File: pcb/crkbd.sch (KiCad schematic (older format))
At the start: 79 parts, among them J1 MJ-4PP-9, J2 OLED, J3 LED, SW1 SW_PUSH, SW10 SW_PUSH, SW11 SW_PUSH, SW12 SW_PUSH, SW13 SW_PUSH, SW14 SW_PUSH, SW15 SW_PUSH, SW16 SW_PUSH, SW17 SW_PUSH, SW18 SW_PUSH, SW19 SW_PUSH, SW2 SW_PUSH, SW20 SW_PUSH, SW21 SW_PUSH, SW3 SW_PUSH, SW4 SW_PUSH, SW5 SW_PUSH, SW6 SW_PUSH, SW7 SW_PUSH, SW8 SW_PUSH, SW9 SW_PUSH, U1 ProMicro

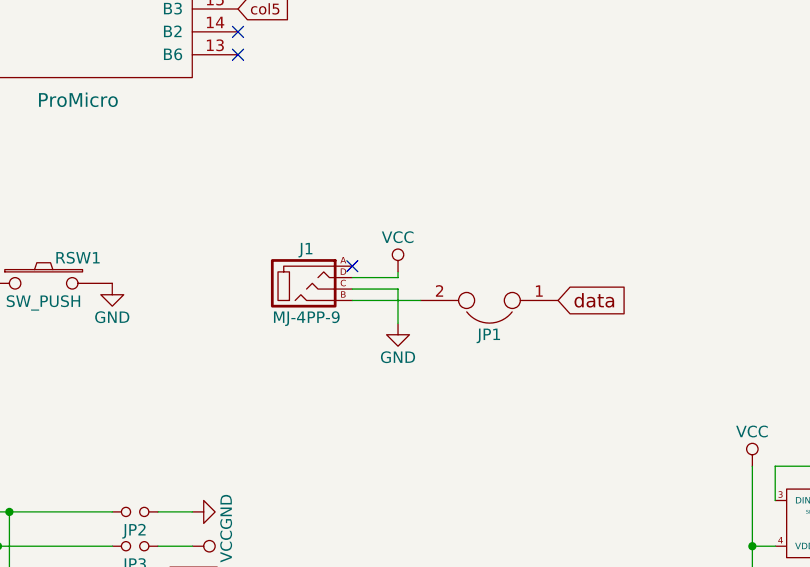
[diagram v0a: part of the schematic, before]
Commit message: Add i2c pin
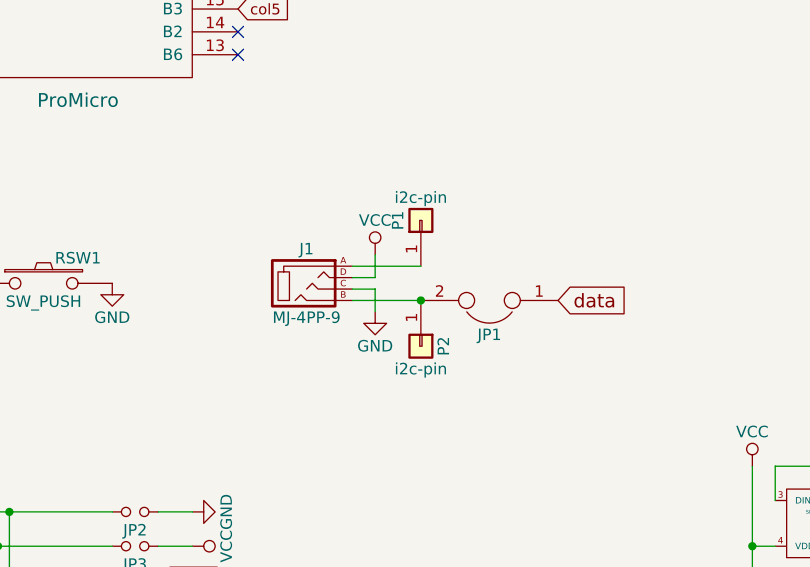
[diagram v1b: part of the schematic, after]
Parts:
- added P1, P2: i2c-pin, kbd:1pin_conn, symbol Conn_01x01
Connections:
- net at J1.B, JP1.2: now also P2.1 (Pin_1)
- net at J1.A: now also P1.1 (Pin_1)
- no-connect marks 7 -> 6
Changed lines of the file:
@@
 L VCC #PWR08
 U 1 1 5A76093E
-P 3200 3250
-F 0 "#PWR08" H 3200 3100 50  0001 C CNN
-F 1 "VCC" H 3200 3400 50  0000 C CNN
-F 2 "" H 3200 3250 50  0001 C CNN
-F 3 "" H 3200 3250 50  0001 C CNN
-	1    3200 3250
+P 3100 3175
+F 0 "#PWR08" H 3100 3025 50  0001 C CNN
+F 1 "VCC" H 3100 3325 50  0000 C CNN
+F 2 "" H 3100 3175 50  0001 C CNN
+F 3 "" H 3100 3175 50  0001 C CNN
+	1    3100 3175
 	1    0    0    -1
 $EndComp
@@
 L GND #PWR09
 U 1 1 5A760ADB
-P 3200 3475
-F 0 "#PWR09" H 3200 3225 50  0001 C CNN
-F 1 "GND" H 3200 3325 50  0000 C CNN
-F 2 "" H 3200 3475 50  0001 C CNN
-F 3 "" H 3200 3475 50  0001 C CNN
-	1    3200 3475
+P 3100 3425
+F 0 "#PWR09" H 3100 3175 50  0001 C CNN
+F 1 "GND" H 3100 3275 50  0000 C CNN
+F 2 "" H 3100 3425 50  0001 C CNN
+F 3 "" H 3100 3425 50  0001 C CNN
+	1    3100 3425
 	1    0    0    -1
 $EndComp
@@
 	1    0    0    -1
 $EndComp
-NoConn ~ 3000 3225
 Wire Wire Line
 	3000 3375 3300 3375
 Wire Wire Line
-	3000 3275 3200 3275
-Wire Wire Line
-	3200 3275 3200 3250
-Wire Wire Line
-	3000 3325 3200 3325
-Wire Wire Line
-	3200 3325 3200 3475
+	3000 3275 3100 3275
+Wire Wire Line
+	3100 3275 3100 3175
+Wire Wire Line
+	3000 3325 3100 3325
+Wire Wire Line
+	3100 3325 3100 3425
 $Comp
 L Conn_01x03 J3
@@
 Wire Wire Line
 	1375 6725 1525 6725
+$Comp
+L Conn_01x01 P2
+U 1 1 5AD20E0A
+P 3300 3575
+F 0 "P2" H 3300 3675 50  0000 C CNN
+F 1 "i2c-pin" V 3400 3575 50  0000 C CNN
+F 2 "kbd:1pin_conn" H 3300 3575 50  0001 C CNN
+F 3 "" H 3300 3575 50  0001 C CNN
+	1    3300 3575
+	0    1    1    0
+$EndComp
+$Comp
+L Conn_01x01 P1
+U 1 1 5AD21C5C
+P 3300 3025
+F 0 "P1" H 3300 3125 50  0000 C CNN
+F 1 "i2c-pin" V 3400 3025 50  0000 C CNN
+F 2 "kbd:1pin_conn" H 3300 3025 50  0001 C CNN
+F 3 "" H 3300 3025 50  0001 C CNN
+	1    3300 3025
+	0    -1   -1   0
+$EndComp
+Wire Wire Line
+	3000 3225 3300 3225
+Connection ~ 3300 3375
 $EndSCHEMATC

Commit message: Reset lines
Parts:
- RSW1: footprint kbd:SW_3.5x6.0_TH -> kbd:ResetSW
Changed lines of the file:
@@
 F 0 "RSW1" H 1800 3410 50  0000 C CNN
 F 1 "SW_PUSH" H 1650 3220 50  0000 C CNN
-F 2 "kbd:SW_3.5x6.0_TH" H 1650 3300 50  0001 C CNN
+F 2 "kbd:ResetSW" H 1650 3300 50  0001 C CNN
 F 3 "" H 1650 3300 50  0000 C CNN
 	1    1650 3300

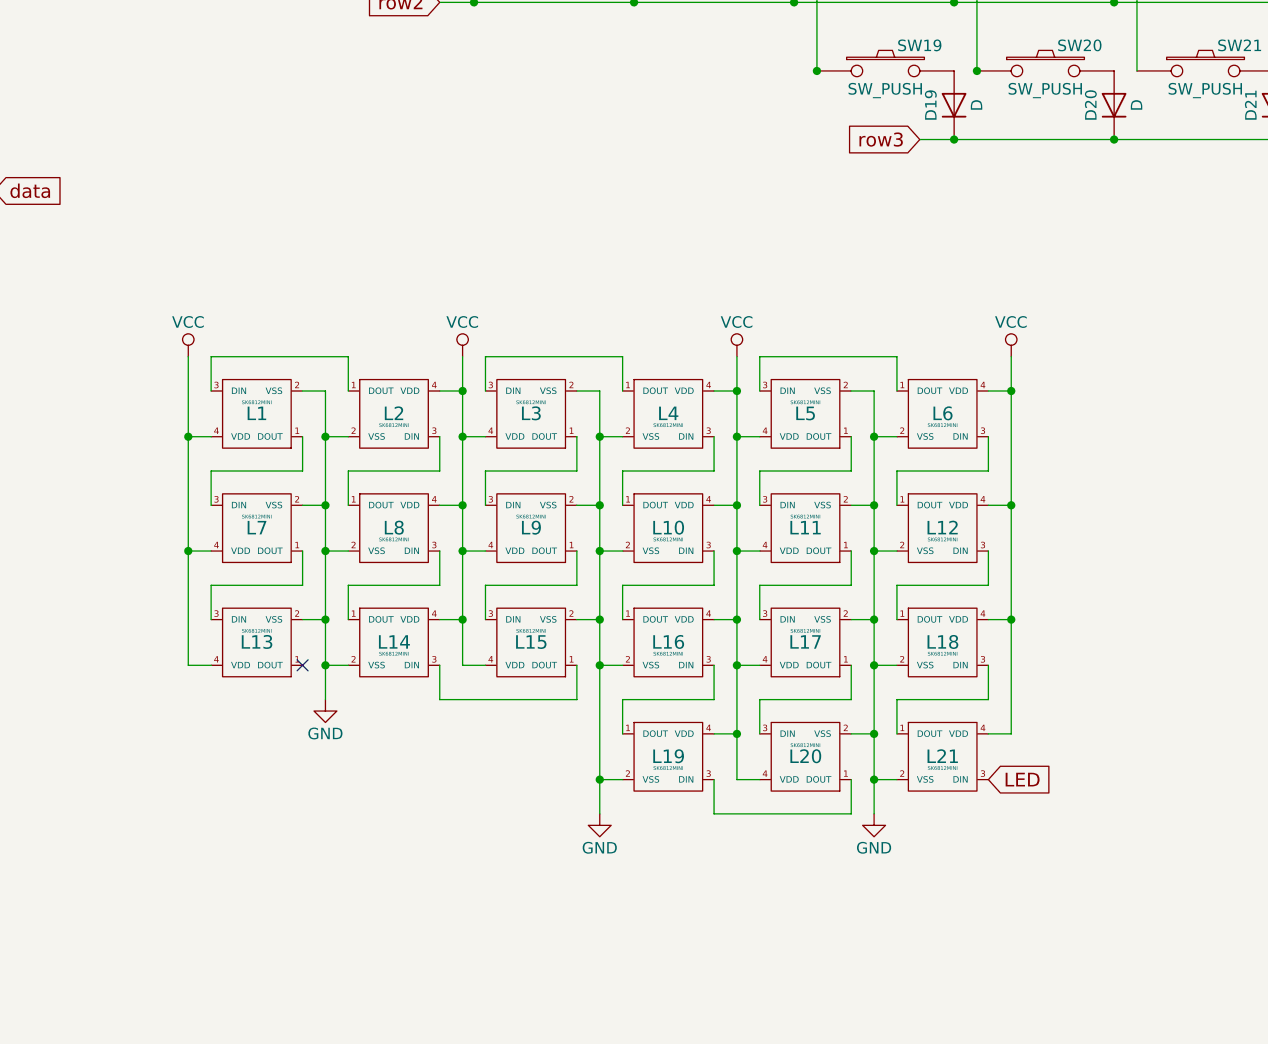
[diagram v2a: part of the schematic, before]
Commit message: Add underground leds
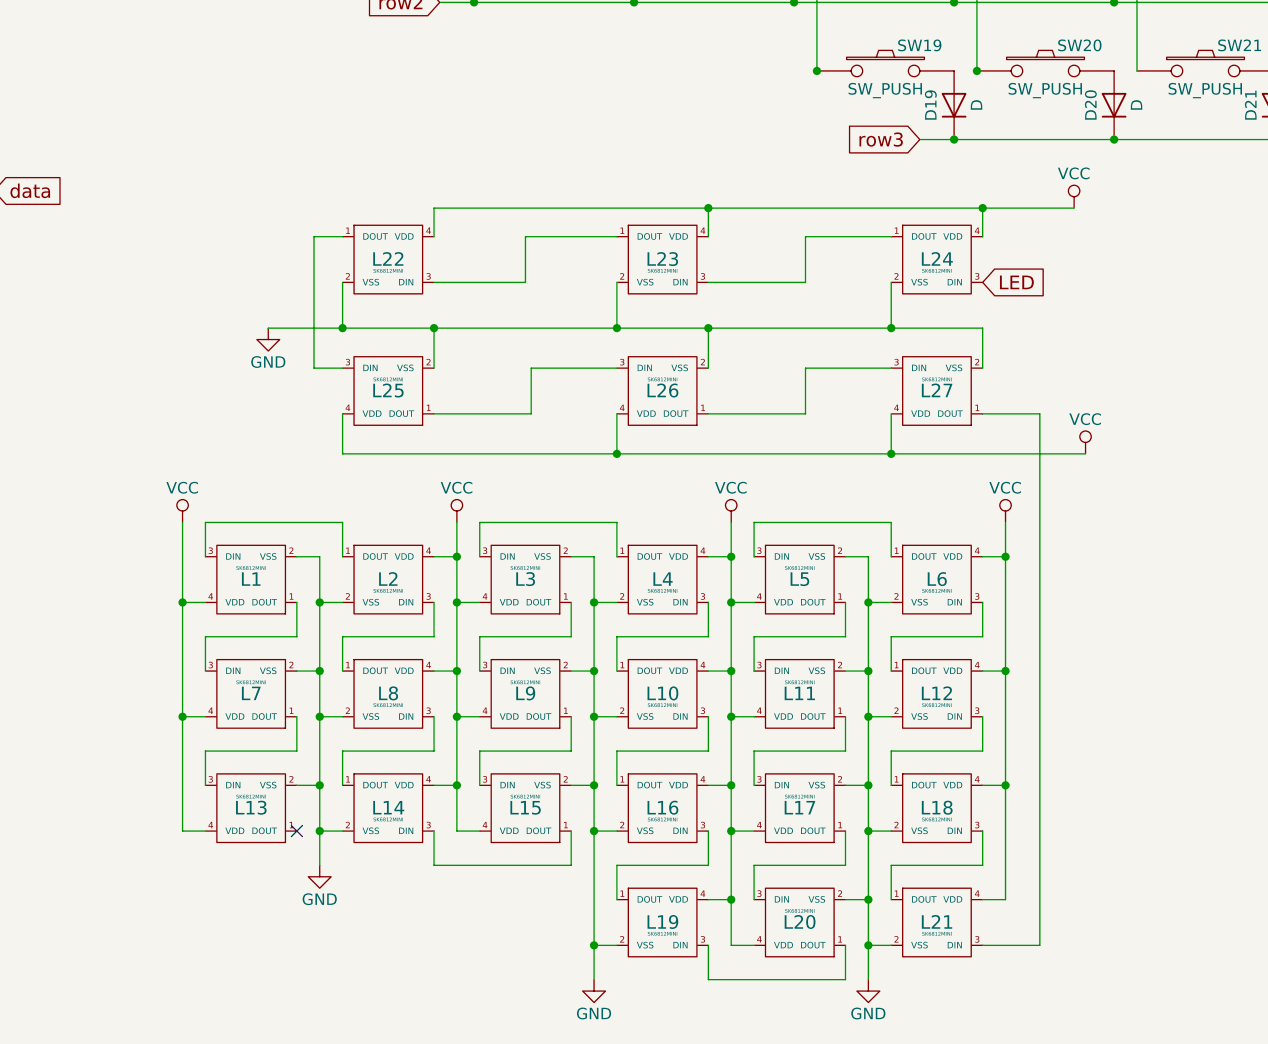
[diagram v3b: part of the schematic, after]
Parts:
- added L22, L23, L24, L25, L26, L27: SK6812MINI, kbd:SK6812MINI_underglow, symbol SK6812MINI
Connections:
- net GND: now also L22.2 (VSS), L23.2 (VSS), L24.2 (VSS), L25.2 (VSS), L26.2 (VSS), L27.2 (VSS)
- net LED: now also L24.3 (DIN); no longer L21.3 (DIN)
- net VCC: now also L22.4 (VDD), L23.4 (VDD), L24.4 (VDD), L25.4 (VDD), L26.4 (VDD), L27.4 (VDD)
- new net: L21.3 (DIN), L27.1 (DOUT)
- new net: L23.3 (DIN), L24.1 (DOUT)
- new net: L22.3 (DIN), L23.1 (DOUT)
- new net: L22.1 (DOUT), L25.3 (DIN)
- new net: L26.1 (DOUT), L27.3 (DIN)
- new net: L25.1 (DOUT), L26.3 (DIN)
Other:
- moved on the sheet: L1, L10, L11, L12, L13, L14, L15, L16, L17, L18, L19, L2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
